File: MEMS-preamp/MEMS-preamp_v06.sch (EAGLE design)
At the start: 47 parts, among them Q1 OPA2134

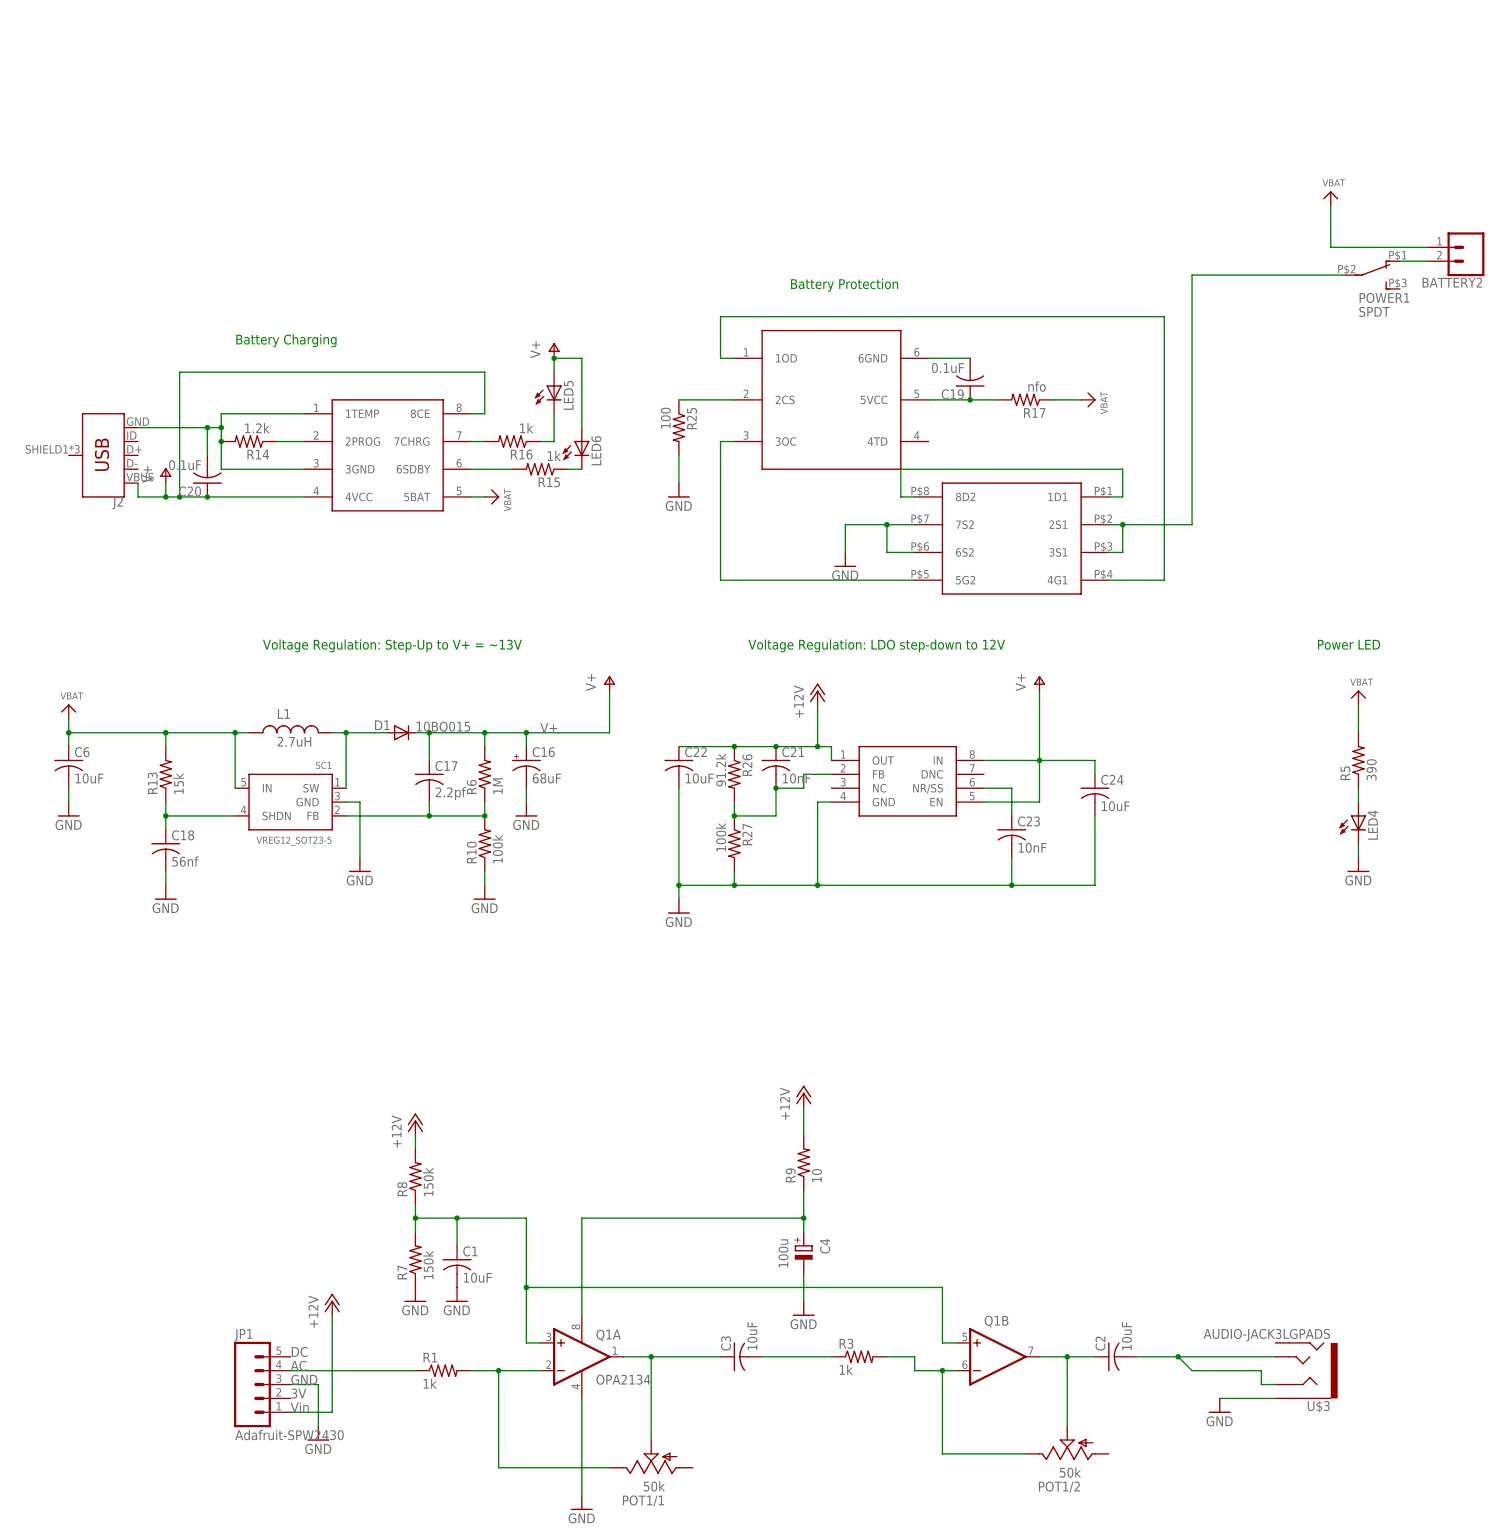
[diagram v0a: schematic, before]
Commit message: mems power fixed
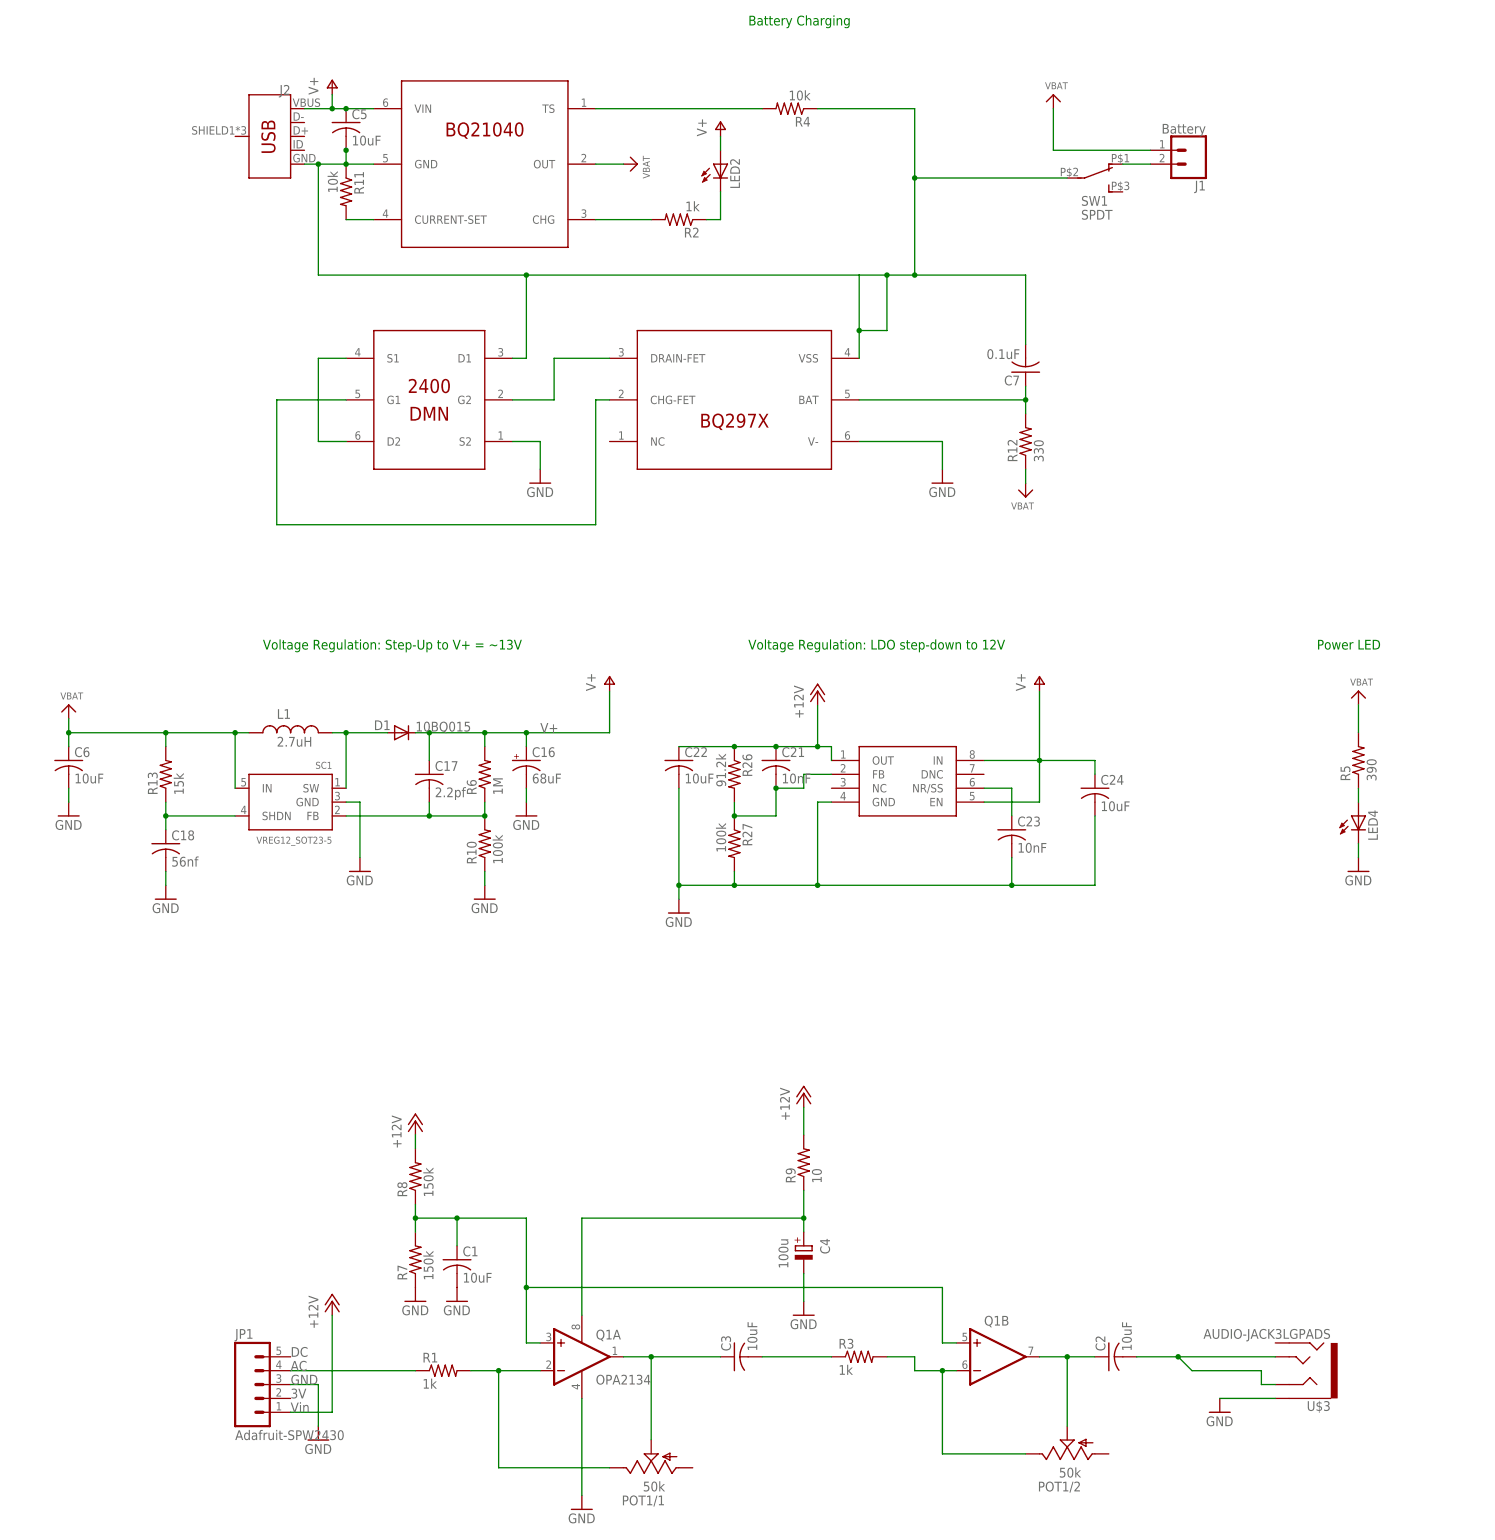
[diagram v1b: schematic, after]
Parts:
- removed BATTERY2: (no value), SparkFun-Connectors:CONN_02LOCK
- removed C19, C20: 0.1uF, adafruit:C-USC0805
- removed DW01A1: DW01A, CMU-ArtFab:DW01A
- removed F8205A1: F8205A, CMU-ArtFab:F8205A
- removed LED5, LED6: (no value), led:LED3MM
- removed POWER1: SPDT, CMU-ArtFab:SWITCH_SPDTCL-SB-12B
- removed R14: 1.2k, CMU-ArtFab:R-US_R0603
- removed R15, R16: 1k, CMU-ArtFab:R-US_R0603
- removed R17: nfo, CMU-ArtFab:R-US_R0603
- removed R25: 100, CMU-ArtFab:R-US_R0603
- removed TP1: TP4056-CHIP, CMU-ArtFab:TP4056-CHIP
- added C5: 10uF, adafruit:C-USC0805K
- added C7: 0.1uF, adafruit:C-USC0805K
- added J1: Battery, SparkFun-Connectors:CONN_02LOCK
- added LED2: (no value), led:LED3MM
- added Q2: BQ21040, CMU-ArtFab:BQ21040-LIPO-CHARGER
- added Q5: BQ297X, CMU-ArtFab:BQ297X-BATTERY-MANAGER
- added Q7: DMN2400, CMU-ArtFab:DUAL-NFET-DMN2400
- added R11, R4: 10k, CMU-ArtFab:R-US_R0805
- added R12: 330, CMU-ArtFab:R-US_R0805
- added R2: 1k, CMU-ArtFab:R-US_R0805
- added SW1: SPDT, CMU-ArtFab:SWITCH_SPDTCL-SB-12B
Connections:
- removed net N$23: LED5.C, R16.1
- removed net N$24: DW01A1.1OD, F8205A1.4G1
- removed net N$25: DW01A1.3OC, F8205A1.5G2
- removed net N$27: C19.1, DW01A1.5VCC, R17.2
- removed net N$31: C19.2, DW01A1.6GND
- removed net N$45: DW01A1.2CS, R25.1
- removed net N$46: F8205A1.1D1, F8205A1.8D2
- new net GND2: C5.2, C7.2, J2.GND, Q2.GND, Q5.VSS, Q7.D1, R11.1, R4.1, SW1.2
- new net N$18: C7.1, Q5.BAT, R12.2
- new net N$20: Q5.CHG-FET, Q7.G1
- net GND: now also Q5.V-, Q7.S2; no longer F8205A1.6S2, F8205A1.7S2, R25.2
- net N$11: now also LED2.C, R2.1; no longer BATTERY2.2, POWER1.1
- net N$15: now also Q2.CHG, R2.2; no longer C20.2, J2.GND, R14.2, TP1.1TEMP, TP1.3GND
- net N$16: now also Q2.TS, R4.2; no longer R14.1, TP1.2PROG
- net N$17: now also Q2.CURRENT-SET, R11.2; no longer R16.2, TP1.7CHRG
- net N$19: now also Q7.D2, Q7.S1; no longer R15.2, TP1.6SDBY
- net N$22: now also Q5.DRAIN-FET, Q7.G2; no longer LED6.C, R15.1
- net N$6: now also J1.2, SW1.1; no longer F8205A1.2S1, F8205A1.3S1, POWER1.2
- net V+: now also C5.1, LED2.A, Q2.VIN; no longer C20.1, LED5.A, LED6.A, TP1.4VCC, TP1.8CE
- net VBAT: now also J1.1, Q2.OUT, R12.1; no longer BATTERY2.1, R17.1, TP1.5BAT
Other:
- note removed: "Battery Protection"
- moved on the sheet: J2
